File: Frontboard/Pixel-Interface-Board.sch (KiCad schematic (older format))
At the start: 29 parts, among them IC1 ATTINY85-P, P1 CONN_02X20, SW1 SW_PUSH, SW10 SW_PUSH, SW11 SW_PUSH, SW12 SW_PUSH, SW2 SW_PUSH, SW3 SW_PUSH, SW4 SW_PUSH, SW5 SW_PUSH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

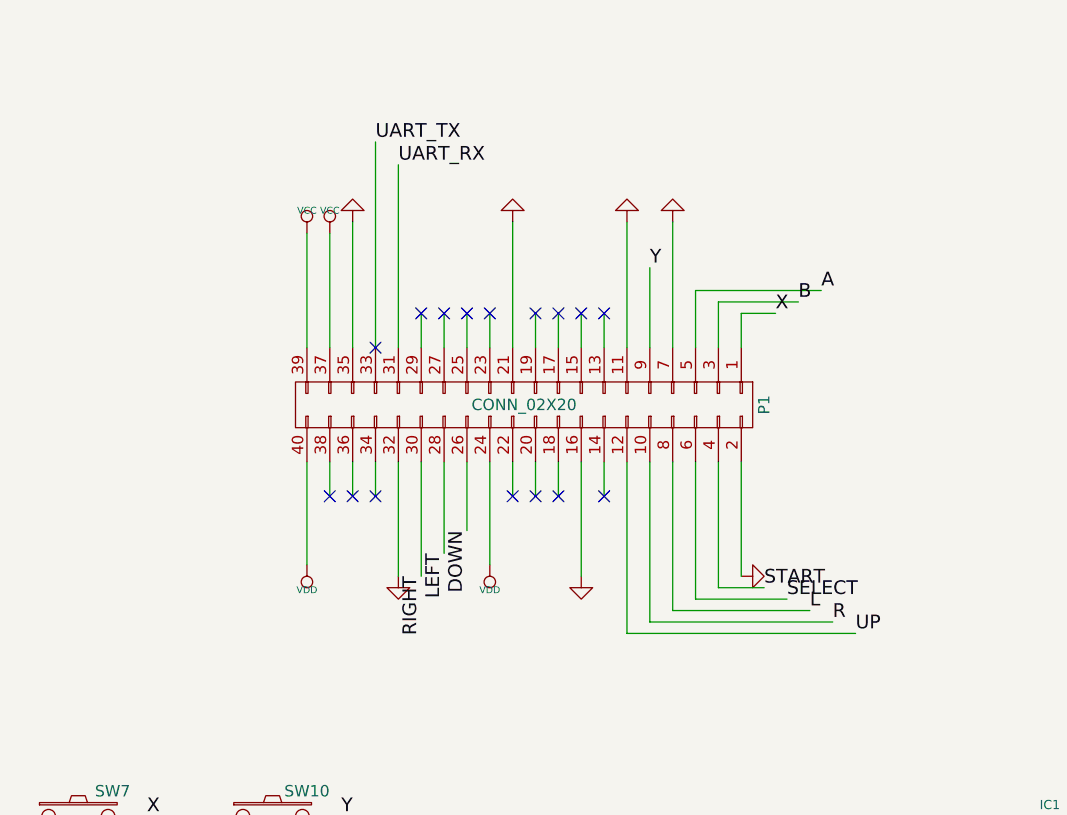
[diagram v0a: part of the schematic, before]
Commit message: Directories moved, .gitignore added.  Major changes to Frontboard design.  Header was completely backwards, fixed now, pins re-arranged. Table coming shortly.
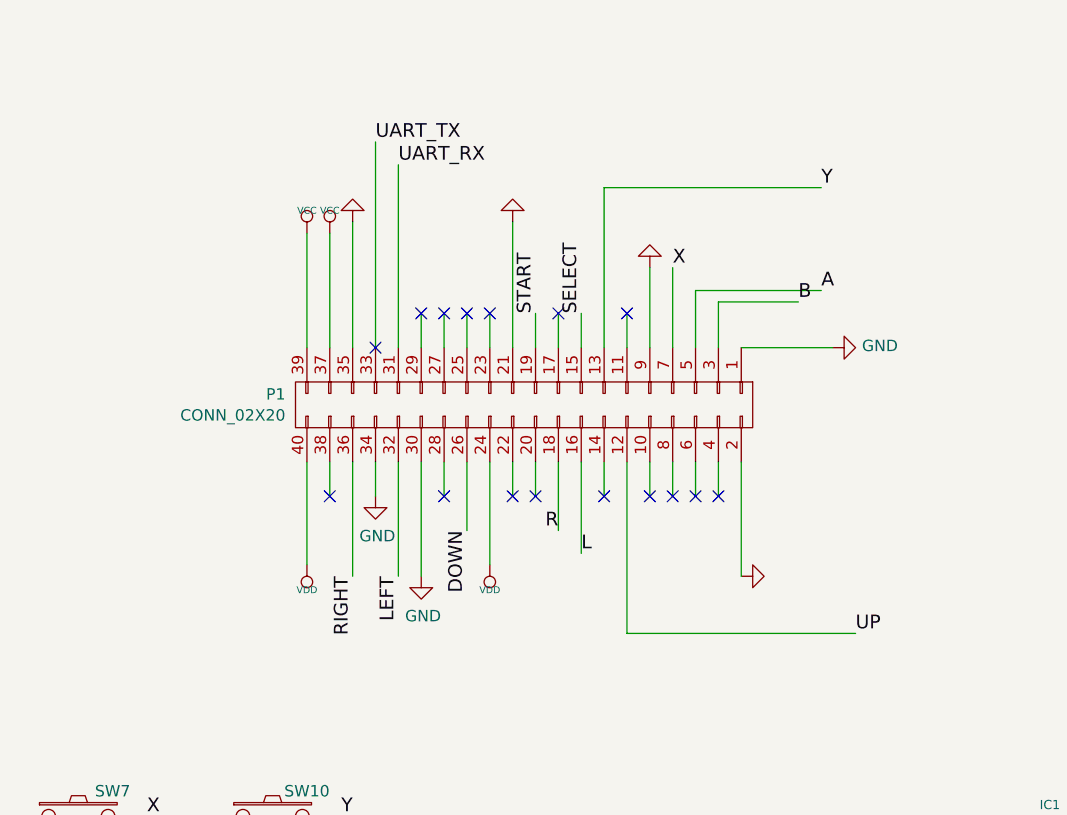
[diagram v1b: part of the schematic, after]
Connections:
- net GND: now also P1.1 (P1), P1.30 (P30), P1.34 (P34), P1.9 (P9); no longer P1.11 (P11), P1.16 (P16), P1.32 (P32), P1.7 (P7)
- net L: now also P1.16 (P16); no longer P1.8 (P8)
- net LEFT: now also P1.32 (P32); no longer P1.28 (P28)
- net R: now also P1.18 (P18); no longer P1.10 (P10)
- net RIGHT: now also P1.36 (P36); no longer P1.30 (P30)
- net SELECT: now also P1.15 (P15); no longer P1.6 (P6)
- net START: now also P1.19 (P19); no longer P1.4 (P4)
- net X: now also P1.7 (P7); no longer P1.1 (P1)
- net Y: now also P1.13 (P13); no longer P1.9 (P9)
